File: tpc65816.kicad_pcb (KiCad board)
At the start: 2 copper layers, 100 x 100 mm, 58 parts, among them J1 Barrel_Jack, Q1 Q_PNP_BCE, Q2 Q_NPN_BCE, U1 74HC00, U10 WD65C22, U11 WD65C22, U2 74LS245, U3 L7805, U4 WD65C816S, U5 74LS573, U6 IS61C5128AS-25QLI, U7 28C256, U8 74F521, U9 74HC00

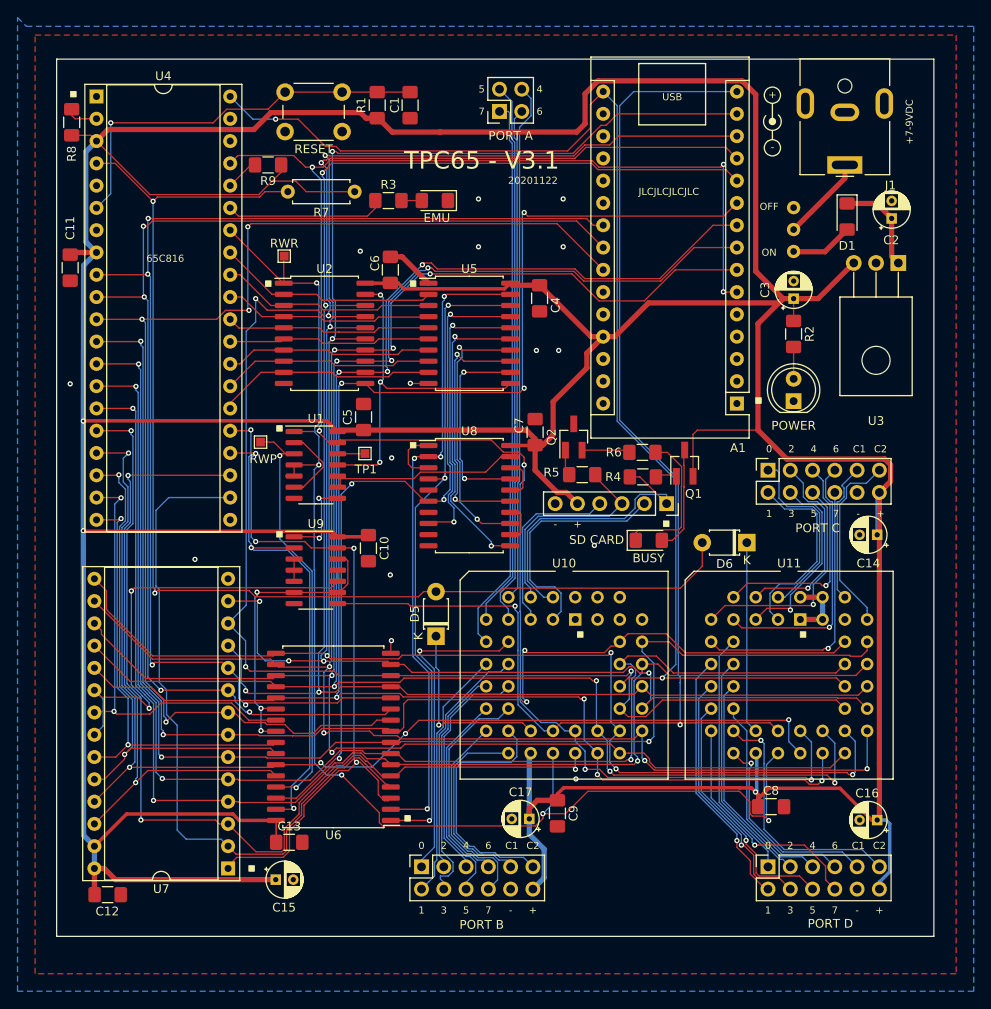
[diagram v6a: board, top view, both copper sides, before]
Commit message: MAJOR FIXES - UNTESTED
Fixes for voltage regulator and barrel jack footprint. Fix for 245 direction. Fix for 65C22 PLCC pin layout. Complete rerouting of board.
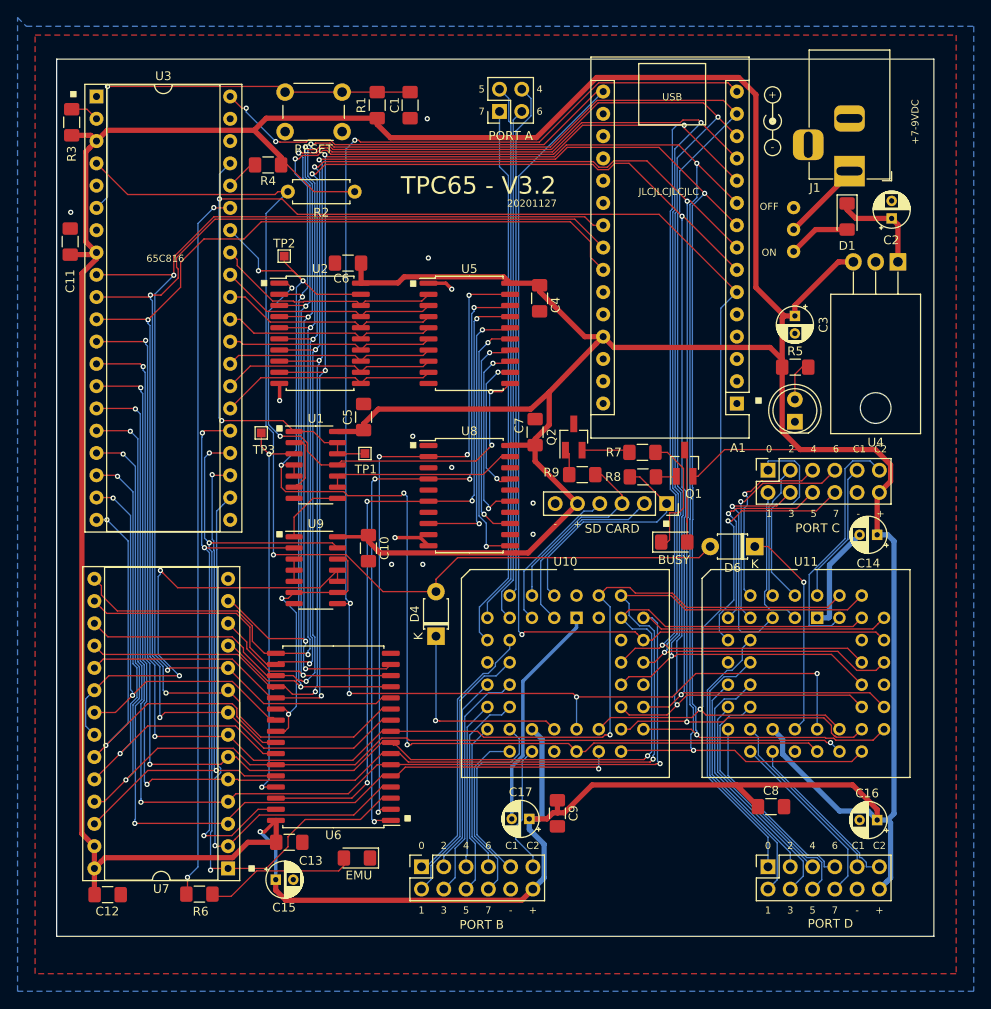
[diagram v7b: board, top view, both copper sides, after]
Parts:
- removed POWER: POWERLED, LED_THT:LED_D5.0mm
- removed the U3 at (200.4, 78.0)
- added  : POWERLED, LED_THT:LED_D5.0mm, F.Cu at (188.6, 96.1)
- added U4: L7805, Package_TO_SOT_THT:TO-220-3_Horizontal_TabDown, F.Cu at (200.4, 77.9)
- J1: footprint Connector_BarrelJack:BarrelJack_CUI_PJ-063AH_Horizontal -> Connector_BarrelJack:BarrelJack_Horizontal
- moved R6 81.9 mm to (120.7, 149.9)
- moved EMU 75.5 mm to (138.7, 145.8)
- moved C6 4.89 mm to (137.7, 78.0), turned to 180 degrees
- moved R5 3.79 mm to (188.7, 89.9), turned to 0 degrees
- moved C11 2.97 mm to (106.0, 75.5), turned to 90 degrees
- moved BUSY 2.91 mm to (174.9, 109.8)
- moved C3 1.98 mm to (188.6, 84.0), turned to 270 degrees
- moved U11 1.93 mm to (191.2, 118.4)
- moved TP3 1.06 mm to (127.8, 97.3)
- moved D6 1.01 mm to (184.0, 110.3)
- moved J1 0.88 mm to (194.8, 67.5), turned to 270 degrees
- moved U2 0.52 mm to (134.5, 86.0)
- moved U10 0.24 mm to (163.7, 118.4)
- renumbered D5 to D4, R7 to R2, R8 to R3, R9 to R4, R2 to R5, R3 to R6, R6 to R7, R4 to R8, R5 to R9, RWR to TP2, RWP to TP3, U4 to U3
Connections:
-   pad 3: Net-(SW2-Pad3) -> (no net)
- A1 pad 1: Net-(A1-Pad1) -> (no net)
- A1 pad 17: Net-(A1-Pad17) -> (no net)
- A1 pad 18: Net-(A1-Pad18) -> (no net)
- A1 pad 19: Net-(A1-Pad19) -> (no net)
- A1 pad 2: Net-(A1-Pad2) -> (no net)
- A1 pad 20: Net-(A1-Pad20) -> (no net)
- A1 pad 21: Net-(A1-Pad21) -> (no net)
- A1 pad 25: Net-(A1-Pad25) -> (no net)
- A1 pad 26: Net-(A1-Pad26) -> (no net)
- A1 pad 28: Net-(A1-Pad28) -> (no net)
- A1 pad 3: Net-(A1-Pad3) -> (no net)
- A1 pad 30: Net-(A1-Pad30) -> (no net)
- A1 pad 5: Net-(A1-Pad5) -> (no net)
- D4 pad 1: Net-(D5-Pad1) (its old number) -> Net-(D4-Pad1)
- PORT C pad 11: Net-(J6-Pad11) -> Net-(J5-Pad11)
- PORT C pad 9: Net-(J6-Pad9) -> Net-(J5-Pad9)
- PORT D pad 11: Net-(J5-Pad11) -> Net-(J6-Pad11)
- PORT D pad 9: Net-(J5-Pad9) -> Net-(J6-Pad9)
- U10 pad 11: /Sheet60C81ED6/PB1 -> (no net)
- U10 pad 12: /Sheet60C81ED6/PB2 -> /Sheet60C81ED6/PB1
- U10 pad 13: /Sheet60C81ED6/PB3 -> /Sheet60C81ED6/PB2
- U10 pad 14: /Sheet60C81ED6/PB4 -> /Sheet60C81ED6/PB3
- U10 pad 15: /Sheet60C81ED6/PB5 -> /Sheet60C81ED6/PB4
- U10 pad 16: /Sheet60C81ED6/PB6 -> /Sheet60C81ED6/PB5
- U10 pad 17: /Sheet60C81ED6/PB7 -> /Sheet60C81ED6/PB6
- U10 pad 18: Net-(J3-Pad9) -> /Sheet60C81ED6/PB7
- U10 pad 19: Net-(J3-Pad11) -> Net-(J3-Pad9)
- U10 pad 20: +5V -> Net-(J3-Pad11)
- U10 pad 21: Net-(D5-Pad1) (its old number) -> +5V
- U10 pad 22: RW_RAW -> (no net)
- U10 pad 23: ~IOCE -> Net-(D4-Pad1)
- U10 pad 24: A7 -> RW_RAW
- U10 pad 25: PH2 -> ~IOCE
- U10 pad 26: DB7 -> A7
- U10 pad 27: DB6 -> PH2
- U10 pad 28: DB5 -> DB7
- U10 pad 29: DB4 -> DB6
- U10 pad 30: DB3 -> DB5
- U10 pad 31: DB2 -> DB4
- U10 pad 32: DB1 -> DB3
- U10 pad 33: DB0 -> (no net)
- U10 pad 34: ~RESET -> DB2
- U10 pad 35: A6 -> DB1
- U10 pad 36: A5 -> DB0
- U10 pad 37: A4 -> ~RESET
- U10 pad 38: A3 -> (no net)
- U10 pad 39: Net-(U10-Pad39) -> A6
- U10 pad 40: Net-(U10-Pad40) -> A5
- U10 pad 41: GND -> A4
- U10 pad 42: GND -> A3
- U10 pad 43: GND -> (no net)
- U10 pad 44: GND -> (no net)
- U11 pad 11: /Sheet60C81ED6/PD1 -> (no net)
- U11 pad 12: /Sheet60C81ED6/PD2 -> /Sheet60C81ED6/PD1
- U11 pad 13: /Sheet60C81ED6/PD3 -> /Sheet60C81ED6/PD2
- U11 pad 14: /Sheet60C81ED6/PD4 -> /Sheet60C81ED6/PD3
- U11 pad 15: /Sheet60C81ED6/PD5 -> /Sheet60C81ED6/PD4
- U11 pad 16: /Sheet60C81ED6/PD6 -> /Sheet60C81ED6/PD5
- U11 pad 17: /Sheet60C81ED6/PD7 -> /Sheet60C81ED6/PD6
- U11 pad 18: Net-(J5-Pad9) -> /Sheet60C81ED6/PD7
- U11 pad 19: Net-(J5-Pad11) -> Net-(J6-Pad9)
- U11 pad 20: +5V -> Net-(J6-Pad11)
- U11 pad 21: Net-(D6-Pad1) -> +5V
- U11 pad 22: RW_RAW -> (no net)
- U11 pad 23: ~IOCE -> Net-(D6-Pad1)
- U11 pad 24: A8 -> RW_RAW
- U11 pad 25: PH2 -> ~IOCE
- U11 pad 26: DB7 -> A8
- U11 pad 27: DB6 -> PH2
- U11 pad 28: DB5 -> DB7
- U11 pad 29: DB4 -> DB6
- U11 pad 30: DB3 -> DB5
- U11 pad 31: DB2 -> DB4
- U11 pad 32: DB1 -> DB3
- U11 pad 33: DB0 -> (no net)
- U11 pad 34: ~RESET -> DB2
- U11 pad 35: A6 -> DB1
- U11 pad 36: A5 -> DB0
- U11 pad 37: A4 -> ~RESET
- U11 pad 38: A3 -> (no net)
- U11 pad 39: Net-(J6-Pad11) -> A6
- U11 pad 40: Net-(J6-Pad9) -> A5
- U11 pad 41: GND -> A4
- U11 pad 42: GND -> A3
- U11 pad 43: GND -> Net-(J5-Pad11)
- U11 pad 44: GND -> Net-(J5-Pad9)
- U2 pad 1: RW_RAW -> Net-(U1-Pad11)
- U2 pad 11: DB7 -> D7
- U2 pad 12: DB6 -> D6
- U2 pad 13: DB5 -> D5
- U2 pad 14: DB4 -> D4
- U2 pad 15: DB3 -> D3
- U2 pad 16: DB2 -> D2
- U2 pad 17: DB1 -> D1
- U2 pad 18: DB0 -> D0
- U2 pad 19: Net-(U1-Pad11) -> RW_RAW
- U2 pad 2: D0 -> DB0
- U2 pad 3: D1 -> DB1
- U2 pad 4: D2 -> DB2
- U2 pad 5: D3 -> DB3
- U2 pad 6: D4 -> DB4
- U2 pad 7: D5 -> DB5
- U2 pad 8: D6 -> DB6
- U2 pad 9: D7 -> DB7
- U3 pad 1: Net-(U4-Pad1) -> (no net)
- U3 pad 38: Net-(U4-Pad38) -> (no net)
- U3 pad 39: Net-(U4-Pad39) -> (no net)
- U3 pad 5: Net-(U4-Pad5) -> (no net)
- U3 pad 7: Net-(U4-Pad7) -> (no net)
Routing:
- net EMU: track 18.2 -> 81.7 mm, vias 0 -> 2
- net DB7: track 199.3 -> 242.1 mm, vias 7 -> 5
- net DB5: track 192.7 -> 233.4 mm
- net DB6: track 198.1 -> 236.4 mm, vias 7 -> 5
- net DB0: track 191.9 -> 230.0 mm, vias 4 -> 5
- net DB2: track 197.6 -> 232.4 mm
- net DB1: track 200.7 -> 230.7 mm
- net DB4: track 200.5 -> 227.8 mm, vias 7 -> 5
- net ~IOCE: track 151.0 -> 176.7 mm, vias 2 -> 5
- net Net-(D4-Pad1): track 0.00 -> 23.6 mm, vias 0 -> 1
- net DB3: track 221.6 -> 244.2 mm, vias 6 -> 4
- net Net-(D5-Pad1) (its old number): track 21.2 -> 0.00 mm, vias 1 -> 0
- net PH2: track 209.8 -> 190.6 mm, vias 7 -> 3
- net +5V: track 630.2 -> 613.3 mm, vias 3 -> 1
- net A12: track 80.0 -> 63.6 mm, vias 0 -> 1
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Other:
- board text added: "20201127"
- board text added: "TPC65 - V3.2"
- board text removed: "20201122"
- board text removed: "TPC65 - V3.1"

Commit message: Fix for bank decoder logic
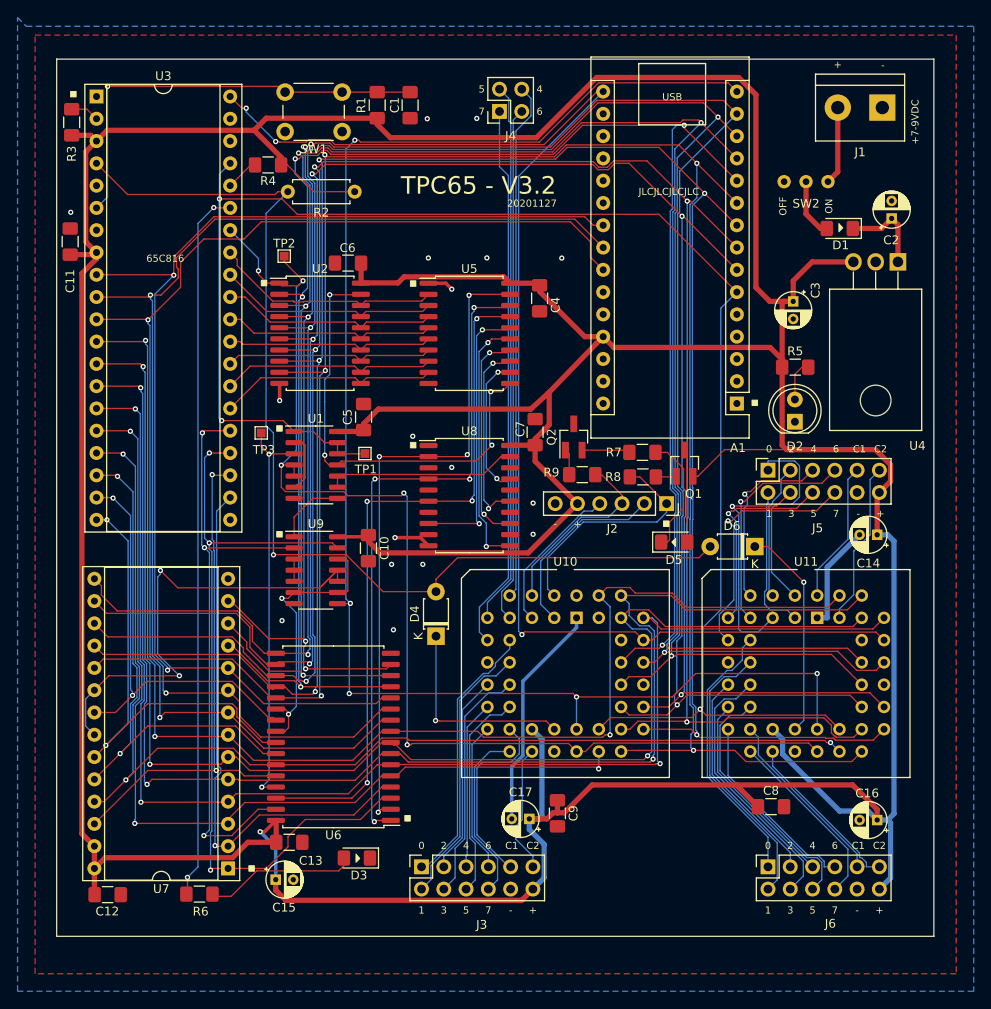
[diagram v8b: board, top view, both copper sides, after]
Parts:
- removed EMU: EMU_STATUS, LED_SMD:LED_1206_3216Metric_Pad1.42x1.75mm_HandSolder
- removed REF**: Symbol_Barrel_Polarity, Symbol:Symbol_Barrel_Polarity
- added D3: EMU_STATUS, LED_SMD:LED_1206_3216Metric_Pad1.42x1.75mm_HandSolder, F.Cu at (138.7, 145.8)
- D2, SW2: renamed from  
- J1: value Barrel_Jack -> Power IN; footprint Connector_BarrelJack:BarrelJack_Horizontal -> TerminalBlock:TerminalBlock_bornier-2_P5.08mm
- J2: renamed from SD CARD
- J3: renamed from PORT B
- J4: renamed from PORT A
- J5: renamed from PORT C
- J6: renamed from PORT D
- U2: value 74LS245 -> 74HC245
- U4: footprint Package_TO_SOT_THT:TO-220-3_Horizontal_TabDown -> Package_TO_SOT_THT:TO-220F-3_Horizontal_TabDown
- U5: value 74LS573 -> 74HC573
- moved J1 8.15 mm to (198.6, 60.3), turned to 180 degrees
- moved SW2 5.64 mm to (189.9, 68.7), turned to 180 degrees
- moved C3 1.66 mm to (188.4, 82.4)
- moved D1 1.60 mm to (193.7, 74.0), turned to 180 degrees
- renumbered BUSY to D5, RESET to SW1
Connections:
- J1 pad 1: Net-(J1-Pad1) -> GND
- J1 pad 2: GND -> Net-(J1-Pad2)
- SW2 pad 1: Net-(D1-Pad2) -> Net-(J1-Pad2)
- SW2 pad 2: Net-(J1-Pad1) -> Net-(D1-Pad2)
- U2 pad 1: Net-(U1-Pad11) -> RW_RAW
- U2 pad 19: RW_RAW -> Net-(U1-Pad11)
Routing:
- net Net-(J5-Pad11): track 28.1 -> 18.7 mm
- net Net-(J1-Pad1): track 9.30 -> 0.00 mm
- net Net-(J1-Pad2): track 0.00 -> 8.91 mm
- net RW_RAW: track 141.1 -> 134.6 mm
- net Net-(U1-Pad11): track 56.0 -> 51.8 mm
- net ~ROM_CS: track 52.5 -> 55.0 mm
- net +5V: track 613.3 -> 615.4 mm
- net Net-(C2-Pad1): track 11.5 -> 10.2 mm
- net Net-(D5-Pad1): track 14.4 -> 13.8 mm
- net GND: track 47.3 -> 47.2 mm, vias 12 -> 17
